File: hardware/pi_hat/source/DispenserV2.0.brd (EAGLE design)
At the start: 65 x 56 mm, 13 parts, among them J10 455-1750-1-ND, J11 455-1750-1-ND, J9 455-1750-1-ND, U2 A4988

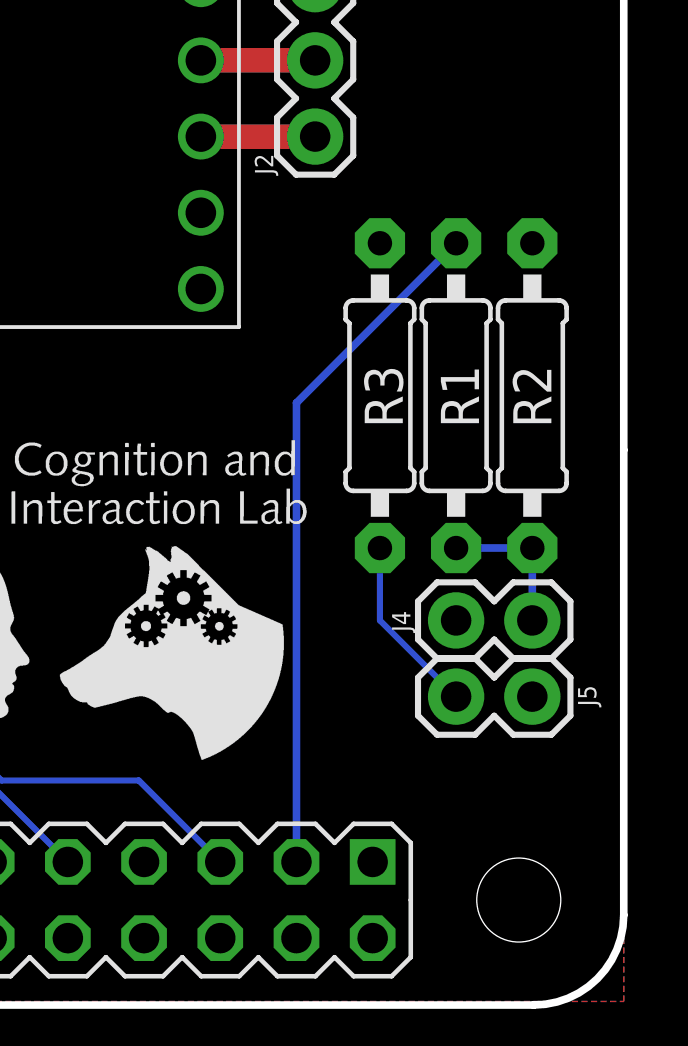
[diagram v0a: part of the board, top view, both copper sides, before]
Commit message: Updating Pi Hat with changes for break sensor
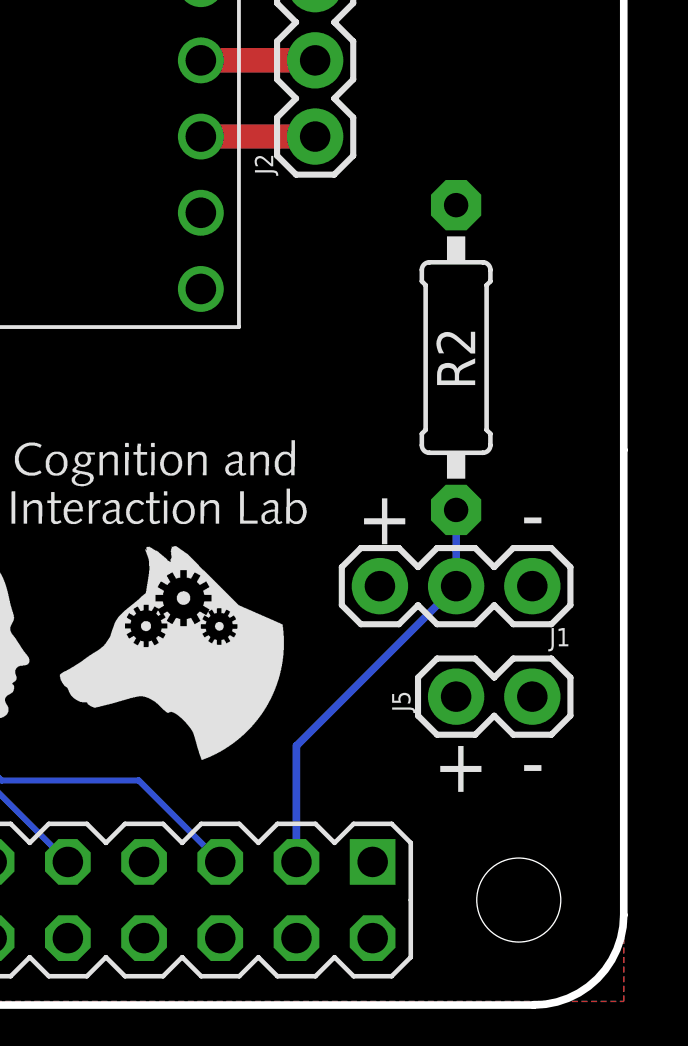
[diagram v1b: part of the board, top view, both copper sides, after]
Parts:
- removed J4: (no value), SparkFun-Connectors:1X02
- removed R1, R3: (no value), adafruit:0207/10
- added J1: 455-1750-1-ND, SparkFun-Connectors:1X03
- moved R2 2.84 mm to (59.2, 21.5)
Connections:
- removed net N$1: J4.2, R1.1, R2.1
- removed net N$2: J5.2, R3.1
- net 3.3V: now also J1.3, J5.2; no longer R3.2
- net BREAK: now also J1.2, R2.1; no longer R1.2
- net GND: now also J1.1; no longer J4.1
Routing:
- net BREAK: track 22.8 -> 13.9 mm
- net N$2: track 6.01 -> 0.00 mm
- net N$1: track 4.95 -> 0.00 mm
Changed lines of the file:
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@@
 <rectangle x1="21.682075" y1="17.370425" x2="21.739225" y2="17.389475" layer="21"/>
 <rectangle x1="34.026475" y1="17.370425" x2="34.540825" y2="17.389475" layer="21"/>
+<text x="55.88" y="15.24" size="1.778" layer="21">+</text>
+<text x="58.42" y="6.985" size="1.778" layer="21">+</text>
+<text x="61.341" y="15.367" size="1.778" layer="21">-</text>
+<text x="61.341" y="7.112" size="1.778" layer="21">-</text>
 </plain>
 <attributes>
@@
 <attribute name="VALUE" x="56.515" y="27.559" size="0.6096" layer="27" font="vector" ratio="20" rot="R90"/>
 </element>
-<element name="J4" library="SparkFun-Connectors" package="1X02" value="" x="59.182" y="12.7" smashed="yes">
-<attribute name="NAME" x="57.658" y="12.319" size="0.6096" layer="25" font="vector" ratio="20" rot="R90"/>
-<attribute name="VALUE" x="57.912" y="10.668" size="0.6096" layer="27" font="vector" ratio="20"/>
-</element>
 <element name="J5" library="SparkFun-Connectors" package="1X02" value="" x="61.722" y="10.16" smashed="yes" rot="R180">
-<attribute name="NAME" x="63.246" y="10.541" size="0.6096" layer="25" font="vector" ratio="20" rot="R270"/>
+<attribute name="NAME" x="57.658" y="9.652" size="0.6096" layer="25" font="vector" ratio="20" rot="R90"/>
 <attribute name="VALUE" x="62.992" y="12.192" size="0.6096" layer="27" font="vector" ratio="20" rot="R180"/>
 </element>
-<element name="R1" library="adafruit" library_urn="urn:adsk.eagle:library:420" package="0207/10" package3d_urn="urn:adsk.eagle:package:6240597/1" value="" x="59.182" y="20.193" smashed="yes" rot="R90">
-<attribute name="NAME" x="58.674" y="21.209" size="1.27" layer="25" font="vector" ratio="10" rot="R270"/>
-<attribute name="VALUE" x="59.8678" y="17.907" size="1.27" layer="27" ratio="10" rot="R90"/>
-</element>
-<element name="R2" library="adafruit" library_urn="urn:adsk.eagle:library:420" package="0207/10" package3d_urn="urn:adsk.eagle:package:6240597/1" value="" x="61.722" y="20.193" smashed="yes" rot="R90">
-<attribute name="NAME" x="61.087" y="21.209" size="1.27" layer="25" font="vector" ratio="10" rot="R270"/>
-<attribute name="VALUE" x="62.4078" y="17.907" size="1.27" layer="27" ratio="10" rot="R90"/>
-</element>
-<element name="R3" library="adafruit" library_urn="urn:adsk.eagle:library:420" package="0207/10" package3d_urn="urn:adsk.eagle:package:6240597/1" value="" x="56.642" y="20.193" smashed="yes" rot="R90">
-<attribute name="NAME" x="56.134" y="21.209" size="1.27" layer="25" font="vector" ratio="10" rot="R270"/>
-<attribute name="VALUE" x="57.277" y="17.9324" size="1.27" layer="27" ratio="10" rot="R90"/>
+<element name="R2" library="adafruit" library_urn="urn:adsk.eagle:library:420" package="0207/10" package3d_urn="urn:adsk.eagle:package:6240597/1" value="" x="59.182" y="21.463" smashed="yes" rot="R90">
+<attribute name="NAME" x="58.547" y="22.479" size="1.27" layer="25" font="vector" ratio="10" rot="R270"/>
+<attribute name="VALUE" x="59.8678" y="19.177" size="1.27" layer="27" ratio="10" rot="R90"/>
+</element>
+<element name="J1" library="SparkFun-Connectors" package="1X03" value="455-1750-1-ND" x="61.722" y="13.843" smashed="yes" rot="R180">
+<attribute name="NAME" x="62.992" y="12.446" size="0.6096" layer="25" font="vector" ratio="20" rot="R180"/>
+<attribute name="PROD_ID" value="XXX-00000" x="61.722" y="13.843" size="1.778" layer="27" rot="R180" display="off"/>
 </element>
 </elements>
@@
 </polygon>
 <contactref element="J5" pad="1"/>
-<contactref element="J4" pad="1"/>
+<contactref element="J1" pad="1"/>
 </signal>
 <signal name="V_USB">
@@
 </polygon>
 <contactref element="R2" pad="2"/>
-<contactref element="R3" pad="2"/>
+<contactref element="J5" pad="2"/>
+<contactref element="J1" pad="3"/>
 </signal>
 <signal name="12V">
@@
 <signal name="BREAK">
 <contactref element="PIE1" pad="3"/>
-<contactref element="R1" pad="2"/>
-<wire x1="59.182" y1="25.273" x2="53.86" y2="19.951" width="0.254" layer="16"/>
-<wire x1="53.86" y1="19.951" x2="53.86" y2="4.65" width="0.254" layer="16"/>
-</signal>
-<signal name="N$1">
-<contactref element="J4" pad="2"/>
-<contactref element="R1" pad="1"/>
 <contactref element="R2" pad="1"/>
-<wire x1="61.722" y1="12.7" x2="61.722" y2="15.113" width="0.254" layer="16"/>
-<wire x1="61.722" y1="15.113" x2="59.182" y2="15.113" width="0.254" layer="16"/>
-</signal>
-<signal name="N$2">
-<contactref element="J5" pad="2"/>
-<contactref element="R3" pad="1"/>
-<wire x1="56.642" y1="15.113" x2="56.642" y2="12.7" width="0.2032" layer="16"/>
-<wire x1="56.642" y1="12.7" x2="59.182" y2="10.16" width="0.2032" layer="16"/>
+<contactref element="J1" pad="2"/>
+<wire x1="59.182" y1="16.383" x2="59.182" y2="13.843" width="0.254" layer="16"/>
+<wire x1="59.182" y1="13.843" x2="53.86" y2="8.521" width="0.254" layer="16"/>
+<wire x1="53.86" y1="8.521" x2="53.86" y2="4.65" width="0.254" layer="16"/>
 </signal>
 </signals>

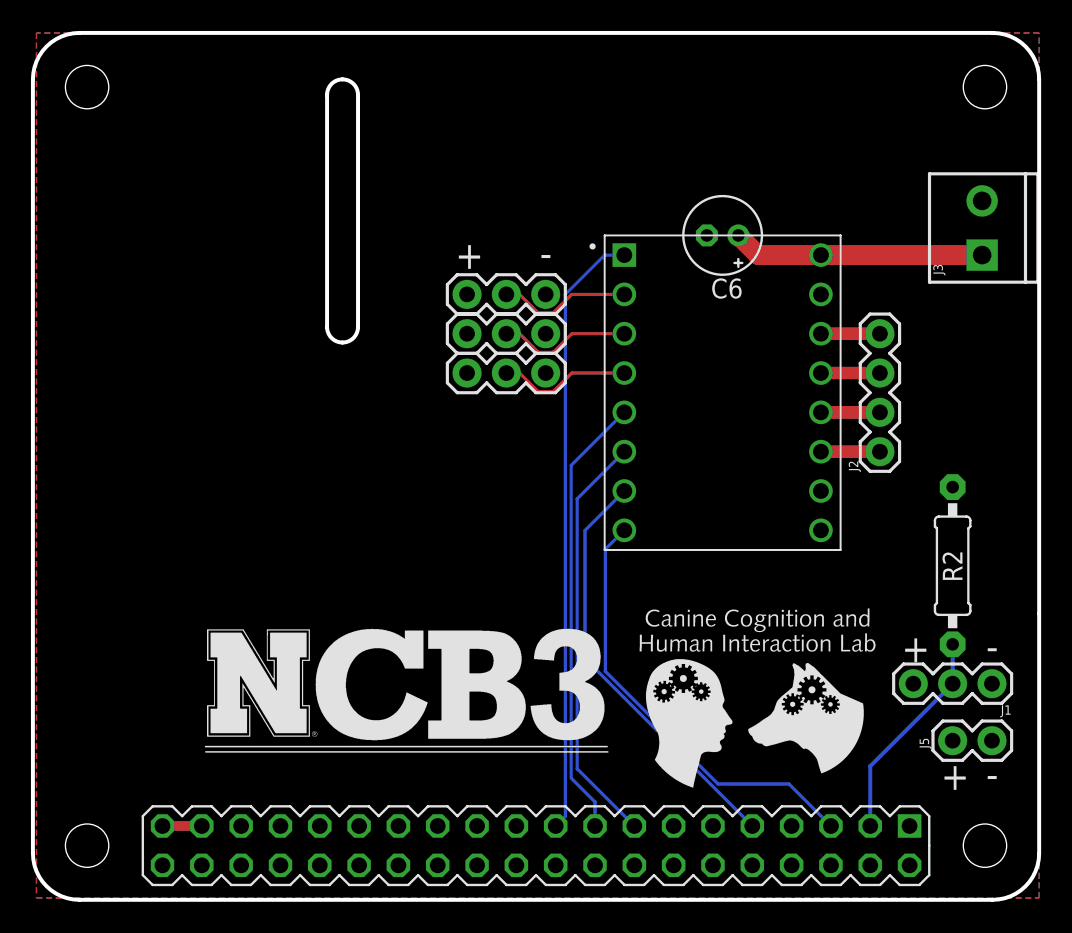
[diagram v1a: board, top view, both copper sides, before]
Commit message: Updated board to include connectors for break sensors
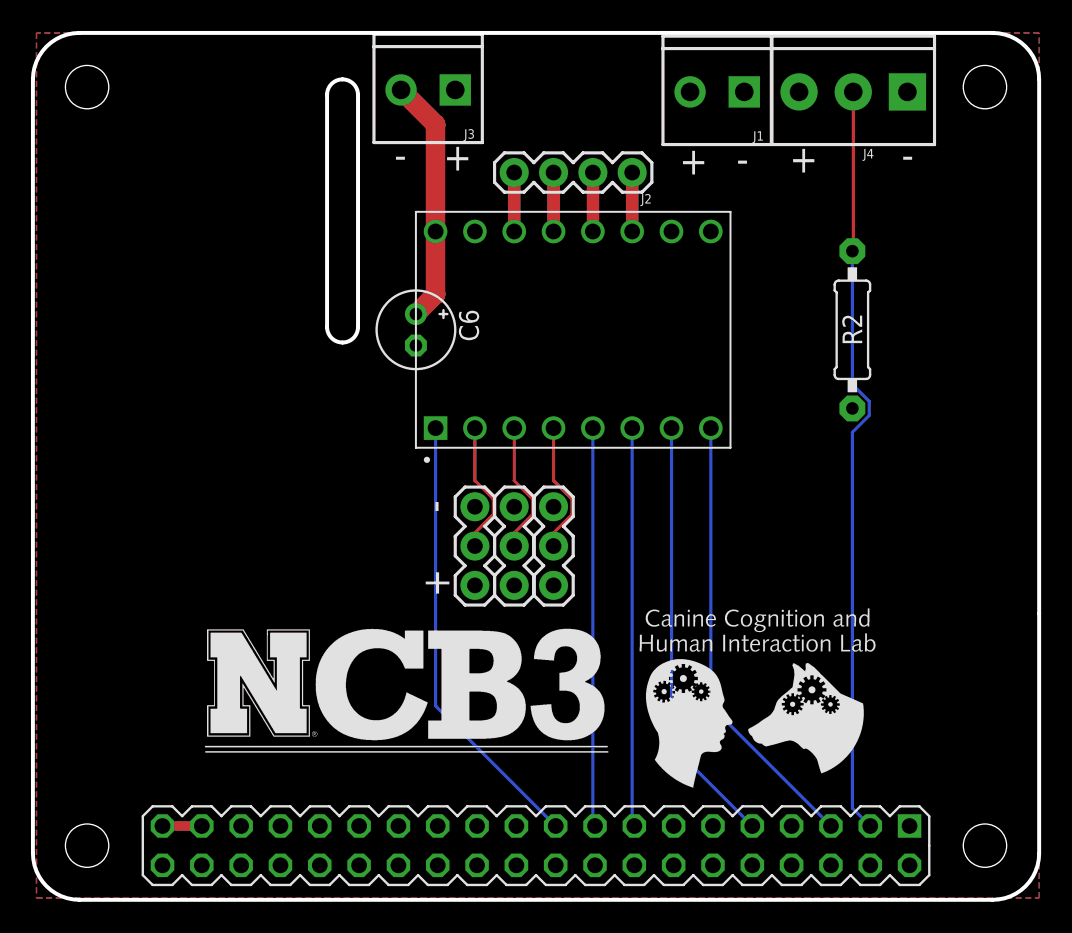
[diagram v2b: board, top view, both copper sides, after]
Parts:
- removed J5: (no value), SparkFun-Connectors:1X02
- added J4: (no value), SparkFun-Connectors:SCREWTERMINAL-3.5MM-3
- J1: value 455-1750-1-ND -> (none); device SparkFun-Connectors:1X03 -> SparkFun-Connectors:SCREWTERMINAL-3.5MM-2
- moved J1 41.4 mm to (45.7, 52.1)
- moved J3 35.7 mm to (27.1, 52.2), turned to 180 degrees
- moved J2 24.1 mm to (38.5, 46.9), turned to 180 degrees
- moved C6 20.7 mm to (24.5, 36.7), turned to 270 degrees
- moved R2 16.6 mm to (52.7, 36.7), turned to 270 degrees
- moved J9 14.5 mm to (28.3, 25.3), turned to 270 degrees
- moved J10 11.4 mm to (30.9, 25.3), turned to 270 degrees
- moved U2 10.5 mm to (34.7, 36.7), turned to 90 degrees
- moved J11 8.65 mm to (33.4, 25.3), turned to 270 degrees
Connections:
- net 12V: now also J3.2; no longer J3.1
- net 3.3V: now also J1.2, J4.3; no longer J1.3, J5.2
- net BREAK: now also J4.2; no longer J1.2
- net GND: now also J3.1, J4.1; no longer J3.2, J5.1
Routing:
- net BREAK: track 13.9 -> 48.8 mm
- net !ENABLE: track 39.5 -> 28.9 mm
- net !RESET: track 28.8 -> 25.8 mm
- net !SLEEP: track 27.0 -> 25.8 mm
- net STEP: track 27.2 -> 27.9 mm
- net DIR: track 28.3 -> 28.9 mm
